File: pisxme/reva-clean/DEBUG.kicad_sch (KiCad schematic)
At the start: 0 parts

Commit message: add native Phase 3 contract connectivity
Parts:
- added X: DEBUG_Contract
- added XDE: DEBUG_Contract, symbol PiSXMeRevAClean:DEBUG_Contract
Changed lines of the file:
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@@
 (kicad_sch (version 20230409) (generator "eeschema")
   (paper "A4")
+    (symbol "PiSXMeRevAClean:DEBUG_Contract"
+      (pin_names (offset 1.0))
+      (exclude_from_sim no)
+      (in_bom yes)
+      (on_board yes)
+      (property "Reference" "X"
+        (at 0 -7.039999999999999 0)
+        (effects (font (size 1.27 1.27))))
+      (property "Value" "DEBUG_Contract"
+        (at 0 7.039999999999999 0)
+        (effects (font (size 1.27 1.27))))
+      (property "Footprint" ""
+        (at 0 0 0)
+        (effects (font (size 1.27 1.27)) (hide yes)))
+      (property "Datasheet" "~"
+        (at 0 0 0)
+        (effects (font (size 1.27 1.27)) (hide yes)))
+      (symbol "DEBUG_Contract_1_1"
+        (rectangle (start -1.27 -5.77) (end 1.27 5.77)
+          (stroke (width 0.254) (type default)) (fill (type background)))
+        (pin passive line
+          (at -5.08 0 0)
+          (length 3.81)
+          (name "UART" (effects (font (size 1.27 1.27))))
+          (number "1" (effects (font (size 1.27 1.27)))))
+        (pin passive line
+          (at -5.08 3 0)
+          (length 3.81)
+          (name "RECOVERY" (effects (font (size 1.27 1.27))))
+          (number "2" (effects (font (size 1.27 1.27)))))
+        (pin passive line
+          (at -5.08 6 0)
+          (length 3.81)
+          (name "POWER_PG_FAULT" (effects (font (size 1.27 1.27))))
+          (number "3" (effects (font (size 1.27 1.27)))))
+        (pin passive line
+          (at -5.08 9 0)
+          (length 3.81)
+          (name "DEBUG_GND" (effects (font (size 1.27 1.27))))
+          (number "4" (effects (font (size 1.27 1.27)))))
+      )
+    )
   (hierarchical_label "UART"
     (shape bidirectional)
@@
     (effects (font (size 1.27 1.27)) (justify left))
 )
-  (sheet_instances (path "/10" (page "10")))
+  (wire
+    (pts (xy 5 10) (xy 19.92 10))
+    (stroke (width 0) (type default))
 )
+  (wire
+    (pts (xy 5 13) (xy 19.92 13))
+    (stroke (width 0) (type default))
+)
+  (wire
+    (pts (xy 5 16) (xy 19.92 16))
+    (stroke (width 0) (type default))
+)
+  (wire
+    (pts (xy 5 19) (xy 19.92 19))
+    (stroke (width 0) (type default))
+)
+  (symbol
+    (lib_id "PiSXMeRevAClean:DEBUG_Contract")
+    (at 25 10 0)
+    (unit 1)
+    (exclude_from_sim no)
+    (in_bom no)
+    (on_board no)
+    (dnp no)
+    (property "Reference" "XDE"
+      (at 25 5 0)
+      (effects (font (size 1.27 1.27))))
+    (property "Value" "DEBUG_Contract"
+      (at 25 18 0)
+      (effects (font (size 1.27 1.27))))
+    (property "Footprint" ""
+      (at 25 10 0)
+      (effects (font (size 1.27 1.27)) (hide yes)))
+    (property "Datasheet" "~"
+      (at 25 10 0)
+      (effects (font (size 1.27 1.27)) (hide yes)))
+    (pin "1")
+    (pin "2")
+    (pin "3")
+    (pin "4")
+    (instances (project "PiSXMe_RevA_Clean"
+      (path "/30000000-0000-0000-0000-000000000000/10000000-0000-0000-0000-00000000000a" (reference "XDE" ) (unit 1))))
+  )
+  (sheet_instances (path "/30000000-0000-0000-0000-000000000000/10000000-0000-0000-0000-00000000000a" (page "10")))
+)

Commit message: close native Phase 3 hierarchy association
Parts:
- removed X: DEBUG_Contract
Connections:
- net DEBUG_GND: now also XDE.4 (DEBUG_GND)
- net POWER_PG_FAULT: now also XDE.3 (POWER_PG_FAULT)
- net RECOVERY: now also XDE.2 (RECOVERY)
- net UART: now also XDE.1 (UART)
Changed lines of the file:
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@@
 (kicad_sch (version 20230409) (generator "eeschema")
   (paper "A4")
-    (symbol "PiSXMeRevAClean:DEBUG_Contract"
-      (pin_names (offset 1.0))
-      (exclude_from_sim no)
-      (in_bom yes)
-      (on_board yes)
-      (property "Reference" "X"
-        (at 0 -7.039999999999999 0)
-        (effects (font (size 1.27 1.27))))
-      (property "Value" "DEBUG_Contract"
-        (at 0 7.039999999999999 0)
-        (effects (font (size 1.27 1.27))))
-      (property "Footprint" ""
-        (at 0 0 0)
-        (effects (font (size 1.27 1.27)) (hide yes)))
-      (property "Datasheet" "~"
-        (at 0 0 0)
-        (effects (font (size 1.27 1.27)) (hide yes)))
-      (symbol "DEBUG_Contract_1_1"
-        (rectangle (start -1.27 -5.77) (end 1.27 5.77)
-          (stroke (width 0.254) (type default)) (fill (type background)))
-        (pin passive line
-          (at -5.08 0 0)
-          (length 3.81)
-          (name "UART" (effects (font (size 1.27 1.27))))
-          (number "1" (effects (font (size 1.27 1.27)))))
-        (pin passive line
-          (at -5.08 3 0)
-          (length 3.81)
-          (name "RECOVERY" (effects (font (size 1.27 1.27))))
-          (number "2" (effects (font (size 1.27 1.27)))))
-        (pin passive line
-          (at -5.08 6 0)
-          (length 3.81)
-          (name "POWER_PG_FAULT" (effects (font (size 1.27 1.27))))
-          (number "3" (effects (font (size 1.27 1.27)))))
-        (pin passive line
-          (at -5.08 9 0)
-          (length 3.81)
-          (name "DEBUG_GND" (effects (font (size 1.27 1.27))))
-          (number "4" (effects (font (size 1.27 1.27)))))
-      )
-    )
   (hierarchical_label "UART"
     (shape bidirectional)
-    (at 5 10 0)
-    (effects (font (size 1.27 1.27)) (justify left))
+    (at 5 10 180)
+    (effects (font (size 1.27 1.27)) (justify right))
 )
   (hierarchical_label "RECOVERY"
     (shape bidirectional)
-    (at 5 13 0)
-    (effects (font (size 1.27 1.27)) (justify left))
+    (at 5 13 180)
+    (effects (font (size 1.27 1.27)) (justify right))
 )
   (hierarchical_label "POWER_PG_FAULT"
     (shape bidirectional)
-    (at 5 16 0)
-    (effects (font (size 1.27 1.27)) (justify left))
+    (at 5 16 180)
+    (effects (font (size 1.27 1.27)) (justify right))
 )
   (hierarchical_label "DEBUG_GND"
     (shape bidirectional)
-    (at 5 19 0)
-    (effects (font (size 1.27 1.27)) (justify left))
+    (at 5 19 180)
+    (effects (font (size 1.27 1.27)) (justify right))
 )
   (wire

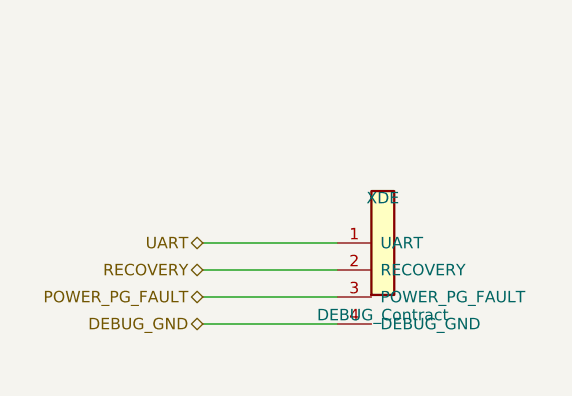
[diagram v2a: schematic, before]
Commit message: stabilize Phase 3 hierarchy netlist references
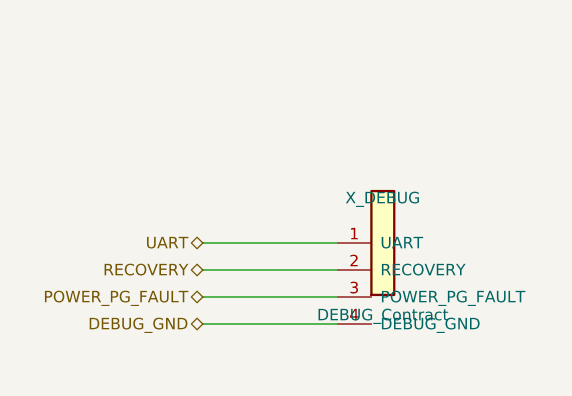
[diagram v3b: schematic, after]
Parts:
- renumbered XDE to X_DEBUG
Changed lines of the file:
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@@
     (on_board no)
     (dnp no)
-    (property "Reference" "XDE"
+    (property "Reference" "X_DEBUG"
       (at 25 5 0)
       (effects (font (size 1.27 1.27))))
@@
     (pin "4")
     (instances (project "PiSXMe_RevA_Clean"
-      (path "/30000000-0000-0000-0000-000000000000/10000000-0000-0000-0000-00000000000a" (reference "XDE" ) (unit 1))))
+      (path "/30000000-0000-0000-0000-000000000000/10000000-0000-0000-0000-00000000000a" (reference "X_DEBUG" ) (unit 1))))
   )
   (sheet_instances (path "/30000000-0000-0000-0000-000000000000/10000000-0000-0000-0000-00000000000a" (page "10")))

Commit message: fix KiCad annotation and netlist export
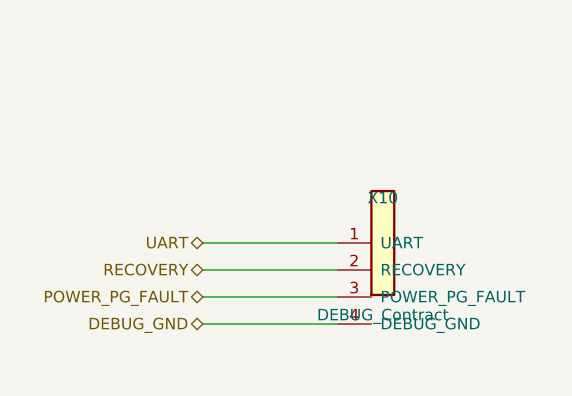
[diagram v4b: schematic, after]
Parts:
- renumbered X_DEBUG to X10
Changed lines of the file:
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@@
     (on_board no)
     (dnp no)
-    (property "Reference" "X_DEBUG"
+    (property "Reference" "X10"
       (at 25 5 0)
       (effects (font (size 1.27 1.27))))
@@
     (pin "4")
     (instances (project "PiSXMe_RevA_Clean"
-      (path "/30000000-0000-0000-0000-000000000000/10000000-0000-0000-0000-00000000000a" (reference "X_DEBUG" ) (unit 1))))
+      (path "/30000000-0000-0000-0000-000000000000/10000000-0000-0000-0000-00000000000a" (reference "X10" ) (unit 1))))
   )
   (sheet_instances (path "/30000000-0000-0000-0000-000000000000/10000000-0000-0000-0000-00000000000a" (page "10")))

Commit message: phase24: promote identity-preserving hierarchy repair
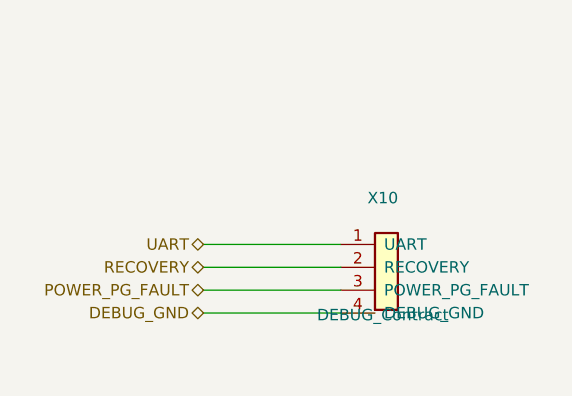
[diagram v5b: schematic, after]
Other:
- moved on the sheet: X10
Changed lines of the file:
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@@
   (hierarchical_label "UART"
     (shape bidirectional)
-    (at 5 10 180)
+    (at 5.08 10.16 180)
     (effects (font (size 1.27 1.27)) (justify right))
 )
   (hierarchical_label "RECOVERY"
     (shape bidirectional)
-    (at 5 13 180)
+    (at 5.08 12.7 180)
     (effects (font (size 1.27 1.27)) (justify right))
 )
   (hierarchical_label "POWER_PG_FAULT"
     (shape bidirectional)
-    (at 5 16 180)
+    (at 5.08 15.24 180)
     (effects (font (size 1.27 1.27)) (justify right))
 )
   (hierarchical_label "DEBUG_GND"
     (shape bidirectional)
-    (at 5 19 180)
+    (at 5.08 17.78 180)
     (effects (font (size 1.27 1.27)) (justify right))
 )
   (wire
-    (pts (xy 5 10) (xy 19.92 10))
+    (pts (xy 5.08 10.16) (xy 20.32 10.16))
     (stroke (width 0) (type default))
 )
   (wire
-    (pts (xy 5 13) (xy 19.92 13))
+    (pts (xy 5.08 12.7) (xy 20.32 12.7))
     (stroke (width 0) (type default))
 )
   (wire
-    (pts (xy 5 16) (xy 19.92 16))
+    (pts (xy 5.08 15.24) (xy 20.32 15.24))
     (stroke (width 0) (type default))
 )
   (wire
-    (pts (xy 5 19) (xy 19.92 19))
+    (pts (xy 5.08 17.78) (xy 20.32 17.78))
     (stroke (width 0) (type default))
 )
   (symbol
     (lib_id "PiSXMeRevAClean:DEBUG_Contract")
-    (at 25 10 0)
+    (at 25.4 10.16 0)
     (unit 1)
     (exclude_from_sim no)
@@
       (effects (font (size 1.27 1.27))))
     (property "Footprint" ""
-      (at 25 10 0)
+      (at 25.4 10.16 0)
       (effects (font (size 1.27 1.27)) (hide yes)))
     (property "Datasheet" "~"
-      (at 25 10 0)
+      (at 25.4 10.16 0)
       (effects (font (size 1.27 1.27)) (hide yes)))
-    (pin "1")
+        (pin "1")
     (pin "2")
     (pin "3")
